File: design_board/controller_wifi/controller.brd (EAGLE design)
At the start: 113.7 x 84 mm, 67 parts, among them IC1 L293D, IC2 7805DT, IC4 7805TV

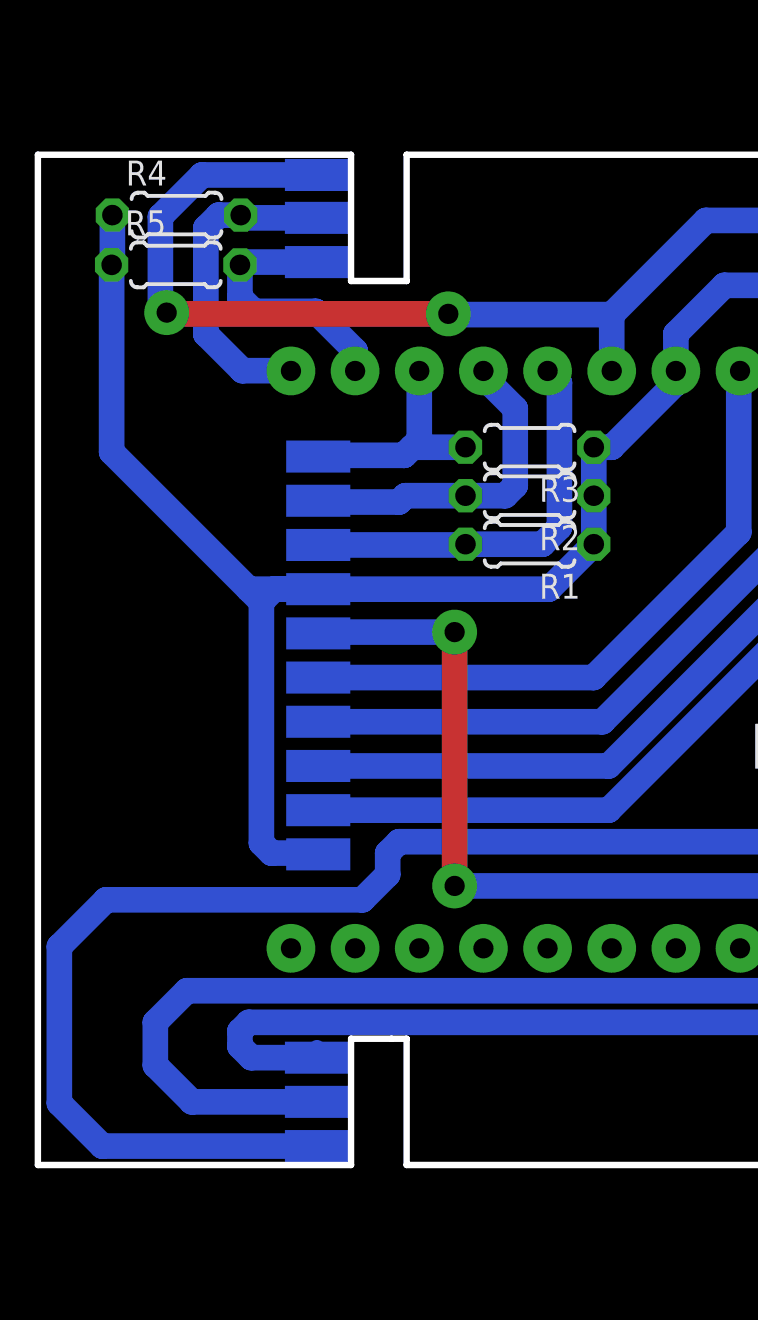
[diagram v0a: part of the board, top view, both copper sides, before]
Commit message: Изменены платы controller.brd и relay.brd - скорректированы зазоры между платами, оp_amp.brd - добавлено отверстие для прокладки проводки между уровнями. Изменена схема сontroller.sch - добавлены номиналы резисторов обвязки оптопар.
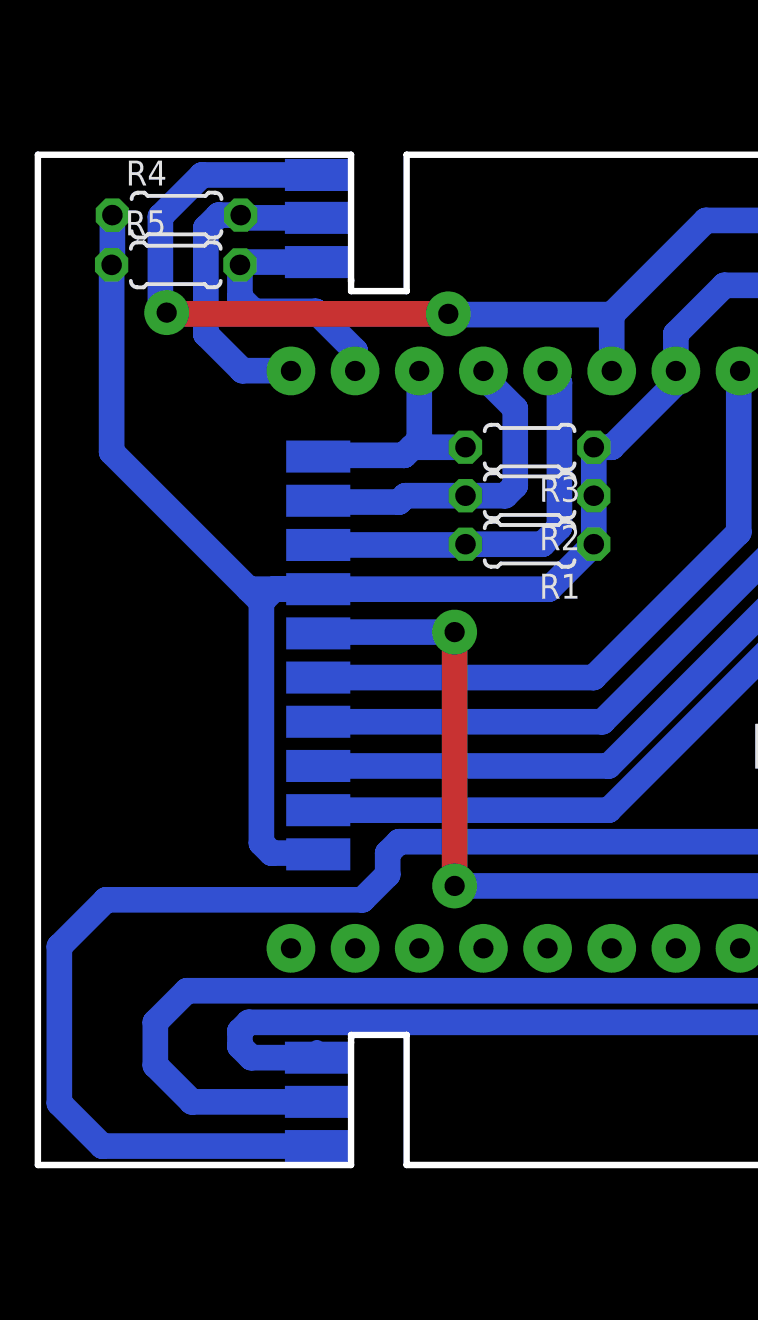
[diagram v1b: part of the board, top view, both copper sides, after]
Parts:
- R1, R2, R3, R4, R5: value (none) -> 4,7 kOm
- R10, R6, R7, R8, R9: value (none) -> 1 kOm
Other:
- outline, holes or cut-outs redrawn
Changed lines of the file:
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@@
 <dimension x1="-62.45" y1="38.25" x2="-62.45" y2="43.25" x3="-73.4" y3="40.75" textsize="1.778" layer="19"/>
 <dimension x1="-62.45" y1="43.25" x2="-62.45" y2="73.25" x3="-70.1" y3="58.25" textsize="1.778" layer="19"/>
-<wire x1="-50.05" y1="73.25" x2="-47.85" y2="73.25" width="0.254" layer="20"/>
 <wire x1="-47.85" y1="78.25" x2="-15.45" y2="78.25" width="0.254" layer="20"/>
 <wire x1="-15.45" y1="38.25" x2="-47.85" y2="38.25" width="0.254" layer="20"/>
 <wire x1="-62.45" y1="78.25" x2="-62.45" y2="38.25" width="0.254" layer="20"/>
-<wire x1="-50.05" y1="43.25" x2="-48.45" y2="43.25" width="0.254" layer="20"/>
 <dimension x1="1.25" y1="16.25" x2="16.25" y2="16.25" x3="8.75" y3="75.4" textsize="1.778" layer="19"/>
 <wire x1="1.25" y1="73.25" x2="19.25" y2="73.25" width="0.254" layer="20"/>
@@
 <wire x1="-50.05" y1="73.25" x2="-50.05" y2="78.25" width="0.254" layer="20"/>
 <wire x1="-50.05" y1="78.25" x2="-62.45" y2="78.25" width="0.254" layer="20"/>
-<wire x1="-50.05" y1="43.25" x2="-50.05" y2="38.25" width="0.254" layer="20"/>
+<wire x1="-50.05" y1="43.25" x2="-50.05" y2="43.1" width="0.254" layer="20"/>
+<wire x1="-50.05" y1="43.1" x2="-50.05" y2="38.25" width="0.254" layer="20"/>
 <wire x1="-50.05" y1="38.25" x2="-62.45" y2="38.25" width="0.254" layer="20"/>
 <dimension x1="-50.05" y1="73.25" x2="-48.45" y2="73.25" x3="-49.25" y3="33.85" textsize="1.778" layer="19"/>
@@
 <dimension x1="1.25" y1="15.7" x2="4.25" y2="15.7" x3="2.75" y3="29.9" textsize="1.778" layer="19"/>
 <dimension x1="-50.05" y1="38.25" x2="-47.85" y2="38.25" x3="-48.95" y3="83.2" textsize="1.778" layer="19"/>
-<wire x1="-47.85" y1="78.25" x2="-47.85" y2="73.25" width="0.254" layer="20"/>
-<wire x1="-47.85" y1="43.25" x2="-48.45" y2="43.25" width="0.254" layer="20"/>
-<wire x1="-47.85" y1="43.25" x2="-47.85" y2="38.25" width="0.254" layer="20"/>
+<wire x1="-47.85" y1="78.25" x2="-47.85" y2="72.85" width="0.254" layer="20"/>
+<wire x1="-47.85" y1="43.4" x2="-47.85" y2="38.25" width="0.254" layer="20"/>
+<wire x1="-50.05" y1="73.3" x2="-50.05" y2="72.85" width="0.254" layer="20"/>
+<wire x1="-50.05" y1="72.85" x2="-47.85" y2="72.85" width="0.254" layer="20"/>
+<wire x1="-47.85" y1="43.4" x2="-50.05" y2="43.4" width="0.254" layer="20"/>
+<wire x1="-50.05" y1="43.4" x2="-50.05" y2="43.25" width="0.254" layer="20"/>
 </plain>
 <attributes>
@@
 <element name="IC2" library="linear4" package="TO252" value="7805DT" x="42.28" y="32.15" rot="MR180"/>
 <element name="NODE_MCU_V1.0" library="ESP12E_DEVKIT" package="ESP12E_DEVKIT" value="ESP12E_DEVKIT" x="-34.65" y="58.26" rot="R90"/>
-<element name="R1" library="resistor" package="0204/5" value="" x="-42.98" y="62.83" rot="R180"/>
-<element name="R2" library="resistor" package="0204/5" value="" x="-42.98" y="64.75" rot="R180"/>
-<element name="R3" library="resistor" package="0204/5" value="" x="-42.98" y="66.67" rot="R180"/>
-<element name="R4" library="resistor" package="0204/5" value="" x="-56.96" y="75.86"/>
-<element name="R5" library="resistor" package="0204/5" value="" x="-56.99" y="73.89"/>
+<element name="R1" library="resistor" package="0204/5" value="4,7 kOm" x="-42.98" y="62.83" rot="R180"/>
+<element name="R2" library="resistor" package="0204/5" value="4,7 kOm" x="-42.98" y="64.75" rot="R180"/>
+<element name="R3" library="resistor" package="0204/5" value="4,7 kOm" x="-42.98" y="66.67" rot="R180"/>
+<element name="R4" library="resistor" package="0204/5" value="4,7 kOm" x="-56.96" y="75.86"/>
+<element name="R5" library="resistor" package="0204/5" value="4,7 kOm" x="-56.99" y="73.89"/>
 <element name="RESET" library="switch-omron" package="B3F-10XX" value="" x="38.94" y="69.41" rot="R180">
 <attribute name="OC_NEWARK" value="36M3542" x="38.94" y="69.41" size="1.778" layer="27" rot="R180" display="off"/>
@@
 <element name="PAD31" library="wirepad" package="SMD1,27-2,54" value="WIREPADSMD1,27-254" x="17.55" y="40.7" rot="MR270"/>
 <element name="PAD32" library="wirepad" package="SMD1,27-2,54" value="WIREPADSMD1,27-254" x="17.55" y="38.95" rot="MR270"/>
-<element name="R6" library="resistor" package="0204V" value="" x="21.35" y="85.9" rot="R90"/>
-<element name="R7" library="resistor" package="0204V" value="" x="11" y="85.9" rot="R90"/>
-<element name="R8" library="resistor" package="0204V" value="" x="43.45" y="86.85" rot="R180"/>
-<element name="R9" library="resistor" package="0204V" value="" x="35.7" y="86.8" rot="R180"/>
-<element name="R10" library="resistor" package="0204V" value="" x="27.9" y="86.85" rot="R180"/>
+<element name="R6" library="resistor" package="0204V" value="1 kOm" x="21.35" y="85.9" rot="R90"/>
+<element name="R7" library="resistor" package="0204V" value="1 kOm" x="11" y="85.9" rot="R90"/>
+<element name="R8" library="resistor" package="0204V" value="1 kOm" x="43.45" y="86.85" rot="R180"/>
+<element name="R9" library="resistor" package="0204V" value="1 kOm" x="35.7" y="86.8" rot="R180"/>
+<element name="R10" library="resistor" package="0204V" value="1 kOm" x="27.9" y="86.85" rot="R180"/>
 <element name="C1" library="resistor" package="E2,5-5" value="" x="-28.25" y="74.35" rot="R270"/>
 <element name="C2" library="resistor" package="E2,5-5" value="" x="34.1" y="40.45" rot="R270"/>
